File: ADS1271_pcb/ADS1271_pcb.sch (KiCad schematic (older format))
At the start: 15 parts, among them U1 ADS1271

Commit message: Se listan los componentes
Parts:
- removed BT?: Battery, symbol Battery
- added BT1: Battery, symbol Battery
- gave numbers to parts that had none: 13
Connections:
- net at U1.15 (VREFN): now also BT1.2 (-)
- net at U1.16 (VREFP): now also BT1.1 (+)
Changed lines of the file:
@@
 $EndComp
 $Comp
-L Battery BT?
-U 1 1 5B1673E9
-P 4050 4850
-F 0 "BT?" H 4150 4950 50  0000 L CNN
-F 1 "Battery" H 4150 4850 50  0000 L CNN
-F 2 "" V 4050 4910 50  0001 C CNN
-F 3 "" V 4050 4910 50  0001 C CNN
-	1    4050 4850
-	0    -1   1    0
-$EndComp
-$Comp
-L Conn_01x06_Male J?
+L Conn_01x06_Male J2
 U 1 1 5B16767B
 P 7500 3050
-F 0 "J?" H 7550 3400 50  0000 C CNN
+F 0 "J2" H 7550 3400 50  0000 C CNN
 F 1 "Conn_01x06_Male" H 7650 2650 50  0000 C CNN
 F 2 "" H 7500 3050 50  0001 C CNN
@@
 CLK
 $Comp
-L R R?
+L R R2
 U 1 1 5B167FA3
 P 6100 2500
-F 0 "R?" V 6180 2500 50  0000 C CNN
+F 0 "R2" V 6180 2500 50  0000 C CNN
 F 1 "50" V 6100 2500 50  0000 C CNN
 F 2 "" V 6030 2500 50  0001 C CNN
@@
 $EndComp
 $Comp
-L R R?
+L R R3
 U 1 1 5B167FD4
 P 6100 2800
-F 0 "R?" V 6180 2800 50  0000 C CNN
+F 0 "R3" V 6180 2800 50  0000 C CNN
 F 1 "50" V 6100 2800 50  0000 C CNN
 F 2 "" V 6030 2800 50  0001 C CNN
@@
 $EndComp
 $Comp
-L R R?
+L R R4
 U 1 1 5B1680B7
 P 6100 3150
-F 0 "R?" V 6180 3150 50  0000 C CNN
+F 0 "R4" V 6180 3150 50  0000 C CNN
 F 1 "50" V 6100 3150 50  0000 C CNN
 F 2 "" V 6030 3150 50  0001 C CNN
@@
 $EndComp
 $Comp
-L R R?
+L R R5
 U 1 1 5B1680E5
 P 6100 3450
-F 0 "R?" V 6180 3450 50  0000 C CNN
+F 0 "R5" V 6180 3450 50  0000 C CNN
 F 1 "50" V 6100 3450 50  0000 C CNN
 F 2 "" V 6030 3450 50  0001 C CNN
@@
 $EndComp
 $Comp
-L R R?
+L R R1
 U 1 1 5B168302
 P 4650 1650
-F 0 "R?" V 4730 1650 50  0000 C CNN
+F 0 "R1" V 4730 1650 50  0000 C CNN
 F 1 "50" V 4650 1650 50  0000 C CNN
 F 2 "" V 4580 1650 50  0001 C CNN
@@
 DVDD
 $Comp
-L C C?
+L C C5
 U 1 1 5B19F27A
 P 3450 3100
-F 0 "C?" H 3475 3200 50  0000 L CNN
+F 0 "C5" H 3475 3200 50  0000 L CNN
 F 1 "1nF" H 3475 3000 50  0000 L CNN
 F 2 "" H 3488 2950 50  0001 C CNN
@@
 $EndComp
 $Comp
-L GNDA #PWR?
+L GNDA #PWR01
 U 1 1 5B1A1201
 P 2800 3700
-F 0 "#PWR?" H 2800 3450 50  0001 C CNN
+F 0 "#PWR01" H 2800 3450 50  0001 C CNN
 F 1 "GNDA" H 2800 3550 50  0000 C CNN
 F 2 "" H 2800 3700 50  0001 C CNN
@@
 $EndComp
 $Comp
-L C C?
+L C C1
 U 1 1 5B1A1242
 P 2800 3550
-F 0 "C?" H 2825 3650 50  0000 L CNN
+F 0 "C1" H 2825 3650 50  0000 L CNN
 F 1 "100pF" H 2900 3550 50  0000 L CNN
 F 2 "" H 2838 3400 50  0001 C CNN
@@
 $EndComp
 $Comp
-L C C?
+L C C2
 U 1 1 5B1A185C
 P 3150 3550
-F 0 "C?" H 3175 3650 50  0000 L CNN
+F 0 "C2" H 3175 3650 50  0000 L CNN
 F 1 "100pF" H 2800 3550 50  0000 L CNN
 F 2 "" H 3188 3400 50  0001 C CNN
@@
 $EndComp
 $Comp
-L GNDA #PWR?
+L GNDA #PWR02
 U 1 1 5B1A18FF
 P 3150 3700
-F 0 "#PWR?" H 3150 3450 50  0001 C CNN
+F 0 "#PWR02" H 3150 3450 50  0001 C CNN
 F 1 "GNDA" H 3150 3550 50  0000 C CNN
 F 2 "" H 3150 3700 50  0001 C CNN
@@
 $EndComp
 $Comp
-L GNDA #PWR?
+L GNDA #PWR03
 U 1 1 5B1A6982
 P 3500 3750
-F 0 "#PWR?" H 3500 3500 50  0001 C CNN
+F 0 "#PWR03" H 3500 3500 50  0001 C CNN
 F 1 "GNDA" H 3500 3600 50  0000 C CNN
 F 2 "" H 3500 3750 50  0001 C CNN
@@
 DGND
 $Comp
-L C C?
+L C C4
 U 1 1 5B1AB96E
 P 3300 2450
-F 0 "C?" H 3325 2550 50  0000 L CNN
+F 0 "C4" H 3325 2550 50  0000 L CNN
 F 1 "10uF" H 3325 2350 50  0000 L CNN
 F 2 "" H 3338 2300 50  0001 C CNN
@@
 $EndComp
 $Comp
-L C C?
+L C C3
 U 1 1 5B1ABAA9
 P 3300 2150
-F 0 "C?" H 3325 2250 50  0000 L CNN
+F 0 "C3" H 3325 2250 50  0000 L CNN
 F 1 "100nF" H 3325 2050 50  0000 L CNN
 F 2 "" H 3338 2000 50  0001 C CNN
@@
 	6350 2500 6250 2500
 Wire Wire Line
-	4250 4850 4250 4200
-Wire Wire Line
-	3850 4850 3850 4200
-Wire Wire Line
-	3850 4200 3900 4200
-Wire Wire Line
 	2600 3300 3600 3300
 Wire Wire Line
@@
 Connection ~ 3550 2450
 $Comp
-L GNDA #PWR?
+L GNDA #PWR04
 U 1 1 5B1ADA12
 P 3000 2600
-F 0 "#PWR?" H 3000 2350 50  0001 C CNN
+F 0 "#PWR04" H 3000 2350 50  0001 C CNN
 F 1 "GNDA" H 3000 2450 50  0000 C CNN
 F 2 "" H 3000 2600 50  0001 C CNN
@@
 $EndComp
 $Comp
-L GNDA #PWR?
+L GNDA #PWR05
 U 1 1 5B1ADA7F
 P 3000 2250
-F 0 "#PWR?" H 3000 2000 50  0001 C CNN
+F 0 "#PWR05" H 3000 2000 50  0001 C CNN
 F 1 "GNDA" H 3000 2100 50  0000 C CNN
 F 2 "" H 3000 2250 50  0001 C CNN
@@
 Wire Wire Line
 	3000 2150 3000 2250
-$Comp
-L +BATT #PWR?
-U 1 1 5B1AF906
-P 3550 1800
-F 0 "#PWR?" H 3550 1650 50  0001 C CNN
-F 1 "+BATT" H 3550 1940 50  0000 C CNN
-F 2 "" H 3550 1800 50  0001 C CNN
-F 3 "" H 3550 1800 50  0001 C CNN
-	1    3550 1800
-	1    0    0    -1
-$EndComp
 Connection ~ 3550 2150
 $Comp
-L Jumper_NC_Dual JP?
+L Jumper_NC_Dual JP1
 U 1 1 5B1B102E
 P 4000 1150
-F 0 "JP?" H 4050 1050 50  0000 L CNN
+F 0 "JP1" H 4050 1050 50  0000 L CNN
 F 1 "Jumper_NC_Dual" H 4000 1250 50  0000 C BNN
 F 2 "" H 4000 1150 50  0001 C CNN
@@
 DGND
 $Comp
-L CONN_01X02_MALE J?
+L CONN_01X02_MALE J1
 U 1 1 5B1A4D1B
 P 2050 3150
-F 0 "J?" H 2050 3325 50  0000 C CNN
+F 0 "J1" H 2050 3325 50  0000 C CNN
 F 1 "CONN_01X02_MALE" H 2050 2950 50  0000 C CNN
 F 2 "" H 2050 3250 50  0001 C CNN
@@
 Text Notes 8150 7650 0    60   ~ 0
 08/06/18\n
+Wire Wire Line
+	4300 4300 4300 4500
+Wire Wire Line
+	4250 4300 4300 4300
+Wire Wire Line
+	4250 4200 4250 4300
+Wire Wire Line
+	3900 4500 3900 4200
+$Comp
+L Battery BT1
+U 1 1 5B417D94
+P 4100 4500
+F 0 "BT1" H 4200 4600 50  0000 L CNN
+F 1 "Battery" H 4200 4500 50  0000 L CNN
+F 2 "" V 4100 4560 50  0001 C CNN
+F 3 "" V 4100 4560 50  0001 C CNN
+	1    4100 4500
+	0    -1   -1   0
+$EndComp
+$Comp
+L +BATT #PWR06
+U 1 1 5B1AF906
+P 3550 1800
+F 0 "#PWR06" H 3550 1650 50  0001 C CNN
+F 1 "+BATT" H 3550 1940 50  0000 C CNN
+F 2 "" H 3550 1800 50  0001 C CNN
+F 3 "" H 3550 1800 50  0001 C CNN
+	1    3550 1800
+	1    0    0    -1
+$EndComp
 $EndSCHEMATC

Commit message: PCB Terminado
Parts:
- removed BT1: Battery, symbol Battery
- removed C3: 100nF, symbol C
- removed C4: 10uF, symbol C
- added C1: 0.33 uf, Capacitors_THT:CP_Radial_D5.0mm_P2.50mm, symbol CP1
- added C2: 0,1 uf, Capacitors_THT:CP_Radial_D5.0mm_P2.50mm, symbol CP1
- added C6: 10 uf, Capacitors_THT:CP_Radial_D5.0mm_P2.50mm, symbol CP1
- added C7: 10uF, Capacitors_THT:CP_Radial_D5.0mm_P2.50mm, symbol C
- added C8: 100nF, Capacitors_THT:CP_Radial_D5.0mm_P2.50mm, symbol C
- added J1: conector +7V, Connectors_Molex:Molex_SPOX-5267_22-03-5025_02x2.54mm_Straight, symbol CONN_01X02_MALE
- added R1: 680, Resistors_THT:R_Axial_DIN0207_L6.3mm_D2.5mm_P5.08mm_Vertical, symbol R
- added U1: LM7805_us, TO_SOT_Packages_THT:TO-220-3_Vertical, symbol LM7805_us
- added U2: LM336z2.5, TO_SOT_Packages_THT:TO-92_Inline_Narrow_Oval, symbol LM336z2.5
- C3: renamed from C1; footprint (none) -> Capacitors_THT:C_Disc_D5.0mm_W2.5mm_P5.00mm
- C4: renamed from C2; footprint (none) -> Capacitors_THT:C_Disc_D5.0mm_W2.5mm_P5.00mm
- C5: footprint (none) -> Capacitors_THT:C_Disc_D5.0mm_W2.5mm_P5.00mm
- J2: renamed from J1; value CONN_01X02_MALE -> CONN_01X02_ent_dif; footprint (none) -> Connectors_Molex:Molex_SPOX-5267_22-03-5025_02x2.54mm_Straight
- J3: renamed from J2; value Conn_01x06_Male -> Conn_01x06_Male_fpga_pins; footprint (none) -> Connectors_Molex:Molex_SPOX-5267_22-03-5065_06x2.54mm_Straight
- JP1: value Jumper_NC_Dual -> Jumper_NC_Dual_selec_modo; footprint (none) -> Connectors_Molex:Molex_SPOX-5267_22-03-5035_03x2.54mm_Straight
- R2: renamed from R1; footprint (none) -> Resistors_THT:R_Axial_DIN0207_L6.3mm_D2.5mm_P5.08mm_Vertical
- R3: renamed from R2; footprint (none) -> Resistors_THT:R_Axial_DIN0207_L6.3mm_D2.5mm_P5.08mm_Vertical
- R4: renamed from R3; footprint (none) -> Resistors_THT:R_Axial_DIN0207_L6.3mm_D2.5mm_P5.08mm_Vertical
- R5: renamed from R4; footprint (none) -> Resistors_THT:R_Axial_DIN0207_L6.3mm_D2.5mm_P5.08mm_Vertical
- R6: renamed from R5; footprint (none) -> Resistors_THT:R_Axial_DIN0207_L6.3mm_D2.5mm_P5.08mm_Vertical
- renumbered U1 to U3
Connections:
- net DGND: now also U3.15 (VREFN), C6.2, C7.1, C8.1, U2.1 (-)
- net DVDD: now also C7.2, C8.2, R1.2
- net GNDA: now also C1.2, C2.2, J1.2, U1.2 (GND)
- net at U3.16 (VREFP): now also C6.1, R1.1, U2.2 (+)
- net +BATT: no longer names the net of U3.4 (AVDD)
- net +BATT: now also C2.1, U1.3 (OUTPUT)
- new net: C1.1, J1.1, U1.1 (INPUT)
- no-connect marks 0 -> 2
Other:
- note removed: "Analizar alimentación analógica: Como la implementamos? Bateria, con tensión regulada?\n"

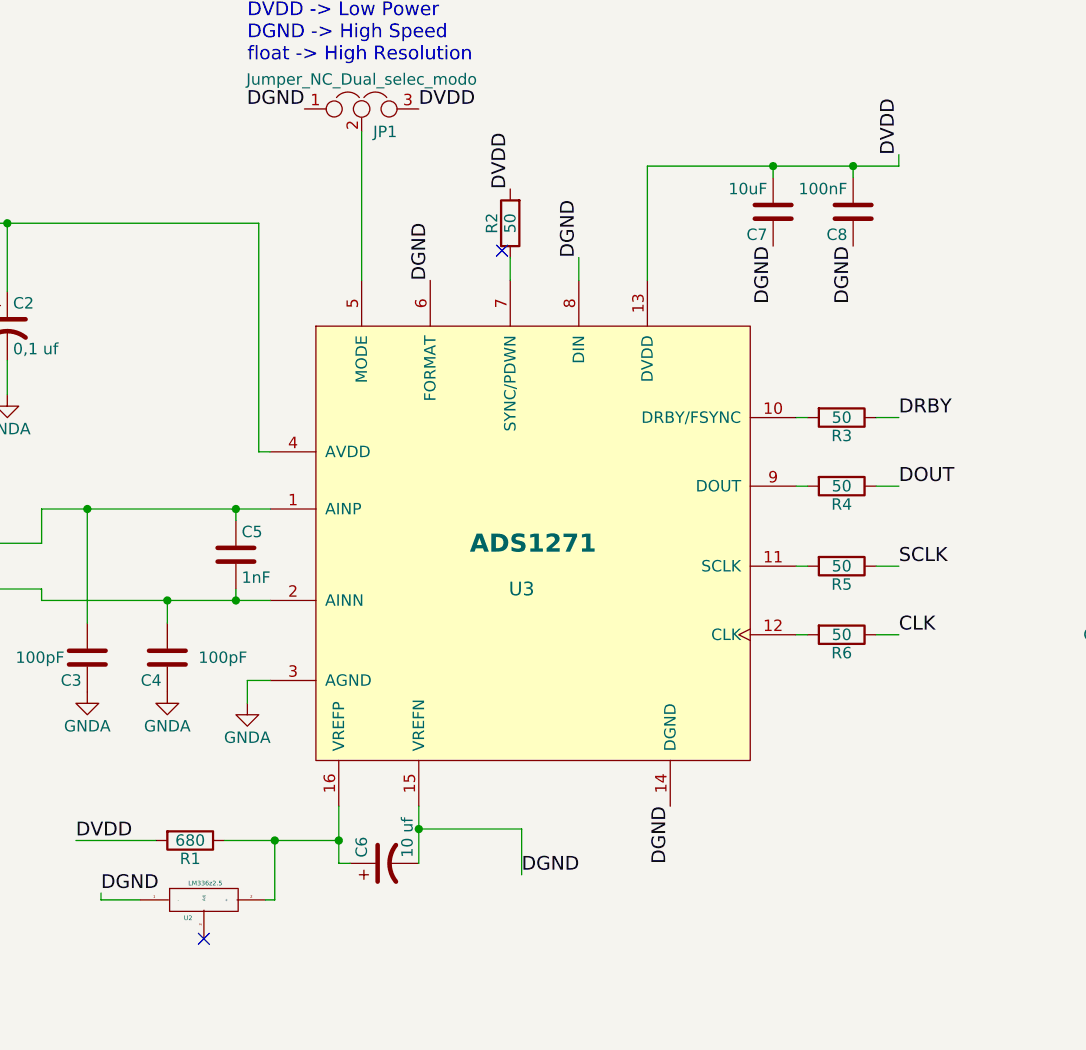
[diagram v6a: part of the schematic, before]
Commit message: Se cambian dos capacitores de ceramica por dos electroliticos, en entrada dvdd (pin 13)
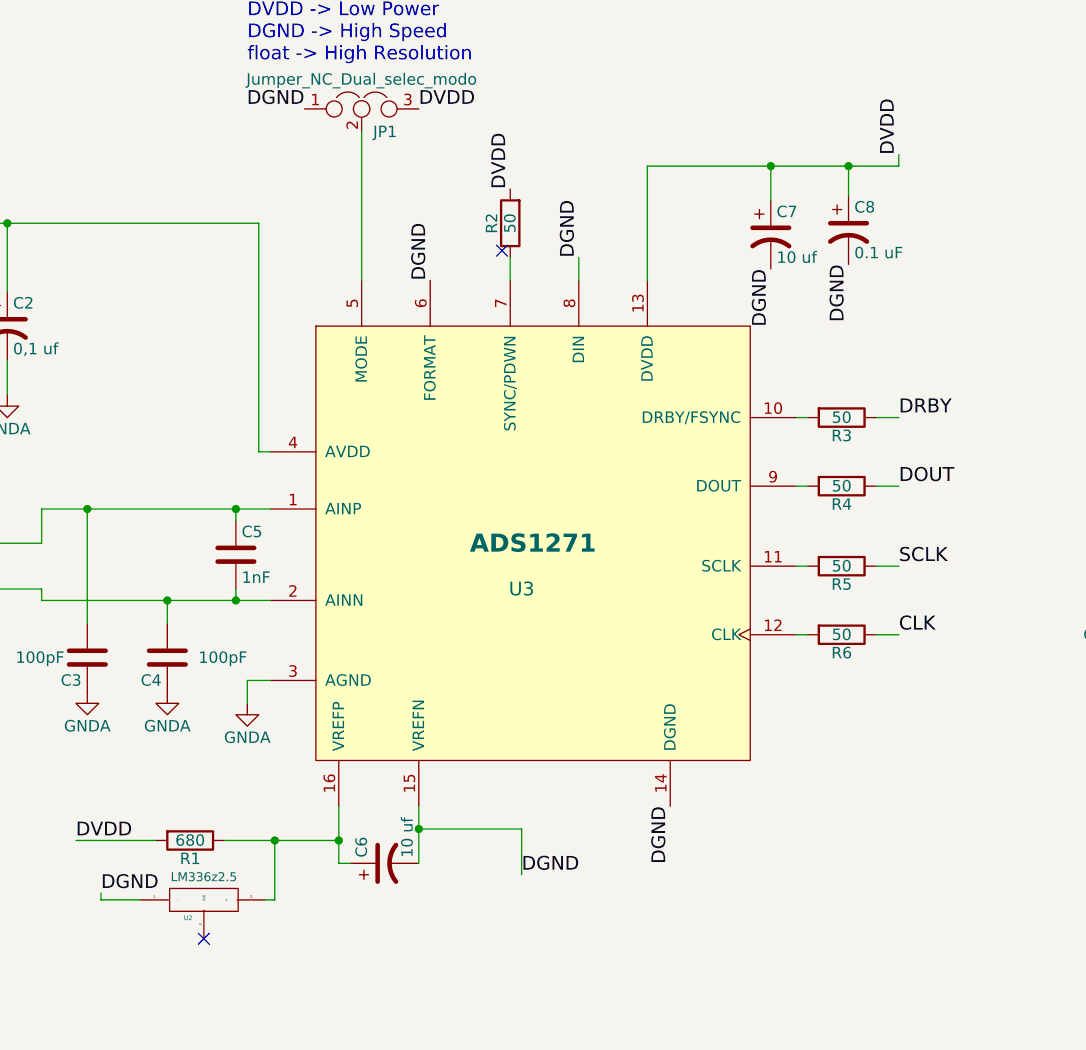
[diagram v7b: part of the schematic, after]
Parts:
- removed C7: 10uF, Capacitors_THT:CP_Radial_D5.0mm_P2.50mm, symbol C
- removed C8: 100nF, Capacitors_THT:CP_Radial_D5.0mm_P2.50mm, symbol C
- added C7: 10 uf, Capacitors_THT:CP_Radial_D5.0mm_P2.50mm, symbol CP1
- added C8: 0.1 uF, Capacitors_THT:CP_Radial_D5.0mm_P2.50mm, symbol CP1
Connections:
- net DGND: now also C7.2, C8.2
- net DVDD: now also C7.1, C8.1
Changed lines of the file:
@@
 Text Notes 8150 7650 0    60   ~ 0
 08/06/18\n
-$Comp
-L C C7
-U 1 1 5B46F37D
-P 5800 1600
-F 0 "C7" H 5825 1700 50  0000 L CNN
-F 1 "10uF" H 5825 1500 50  0000 L CNN
-F 2 "Capacitors_THT:CP_Radial_D5.0mm_P2.50mm" H 5838 1450 50  0001 C CNN
-F 3 "" H 5800 1600 50  0001 C CNN
-	1    5800 1600
-	-1   0    0    1
-$EndComp
-$Comp
-L C C8
-U 1 1 5B46F720
-P 6150 1600
-F 0 "C8" H 6175 1700 50  0000 L CNN
-F 1 "100nF" H 6175 1500 50  0000 L CNN
-F 2 "Capacitors_THT:CP_Radial_D5.0mm_P2.50mm" H 6188 1450 50  0001 C CNN
-F 3 "" H 6150 1600 50  0001 C CNN
-	1    6150 1600
-	-1   0    0    1
-$EndComp
-Text Label 5800 1750 3    60   ~ 0
-DGND
-Text Label 6150 1750 3    60   ~ 0
+Text Label 5790 1850 3    60   ~ 0
+DGND
+Text Label 6130 1830 3    60   ~ 0
 DGND
 $Comp
@@
 P 3310 4610
 F 0 "U2" H 3241 4531 20  0000 C CNN
-F 1 "LM336z2.5" H 3316 4683 20  0000 C CNN
+F 1 "LM336z2.5" H 3310 4710 39  0000 C CNN
 F 2 "TO_SOT_Packages_THT:TO-92_Inline_Narrow_Oval" H 3310 4610 60  0001 C CNN
 F 3 "" H 3310 4610 60  0001 C CNN
@@
 	2800 2900 2800 3400
 Wire Wire Line
-	5800 1450 5800 1400
-Wire Wire Line
 	5250 1400 6350 1400
 Wire Wire Line
-	6150 1400 6150 1450
-Wire Wire Line
 	5250 1400 5250 1900
-Connection ~ 5800 1400
 Wire Wire Line
 	6350 1400 6350 1350
-Connection ~ 6150 1400
 Wire Wire Line
 	3900 4450 3950 4450
@@
 Wire Wire Line
 	4950 1800 4950 1900
+$Comp
+L CP1 C7
+U 1 1 5C7674F1
+P 5790 1700
+F 0 "C7" H 5815 1800 50  0000 L CNN
+F 1 "10 uf" H 5815 1600 50  0000 L CNN
+F 2 "Capacitors_THT:CP_Radial_D5.0mm_P2.50mm" H 5790 1700 50  0001 C CNN
+F 3 "" H 5790 1700 50  0001 C CNN
+	1    5790 1700
+	1    0    0    -1
+$EndComp
+$Comp
+L CP1 C8
+U 1 1 5C767748
+P 6130 1680
+F 0 "C8" H 6155 1780 50  0000 L CNN
+F 1 "0.1 uF" H 6155 1580 50  0000 L CNN
+F 2 "Capacitors_THT:CP_Radial_D5.0mm_P2.50mm" H 6130 1680 50  0001 C CNN
+F 3 "" H 6130 1680 50  0001 C CNN
+	1    6130 1680
+	1    0    0    -1
+$EndComp
+Wire Wire Line
+	5790 1550 5790 1400
+Connection ~ 5790 1400
+Wire Wire Line
+	6130 1530 6130 1400
+Connection ~ 6130 1400
 $EndSCHEMATC
